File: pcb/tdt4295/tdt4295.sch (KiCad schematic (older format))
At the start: 50 parts

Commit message: minor schematic fixes
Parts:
- gave numbers to parts that had none: 50
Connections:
- net GPIO_LED4 is gone; now on net GPIO_LED3: U101.44 (PE7)
- net GPIO_LED0: now also U101.41 (PE4)
- net GPIO_LED1: now also U101.42 (PE5); no longer U101.41 (PE4)
- net GPIO_LED2: now also U101.43 (PE6); no longer U101.42 (PE5)
- net GPIO_LED3: no longer U101.43 (PE6)
- no-connect marks 16 -> 17

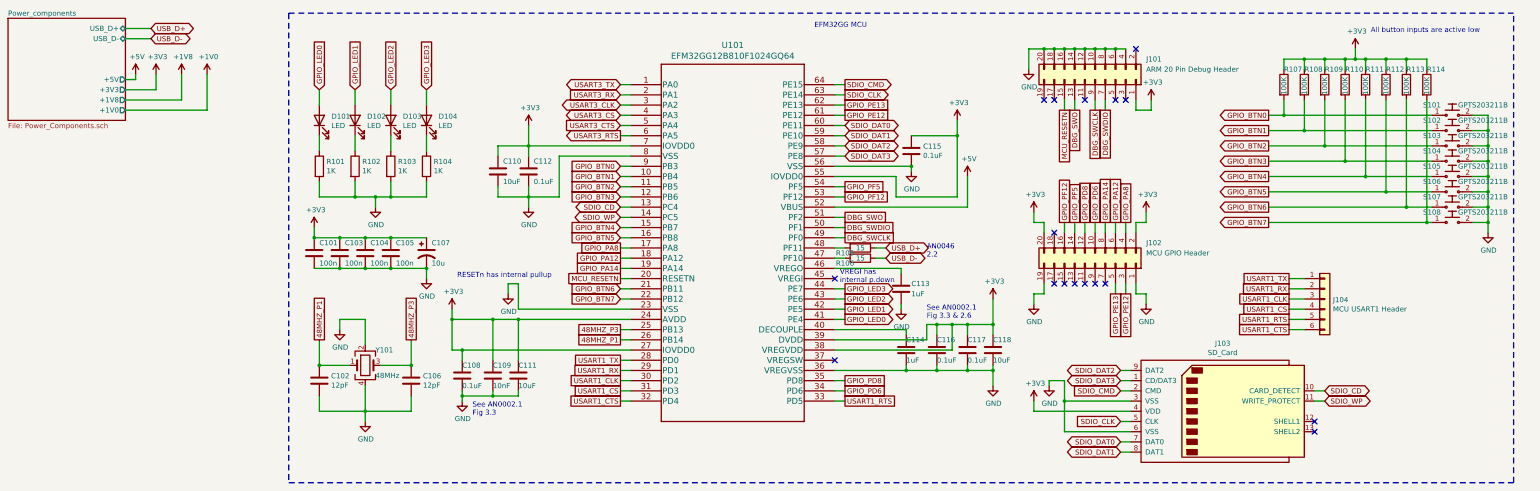
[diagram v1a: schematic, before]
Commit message: Replace PB4-7 with joysticks
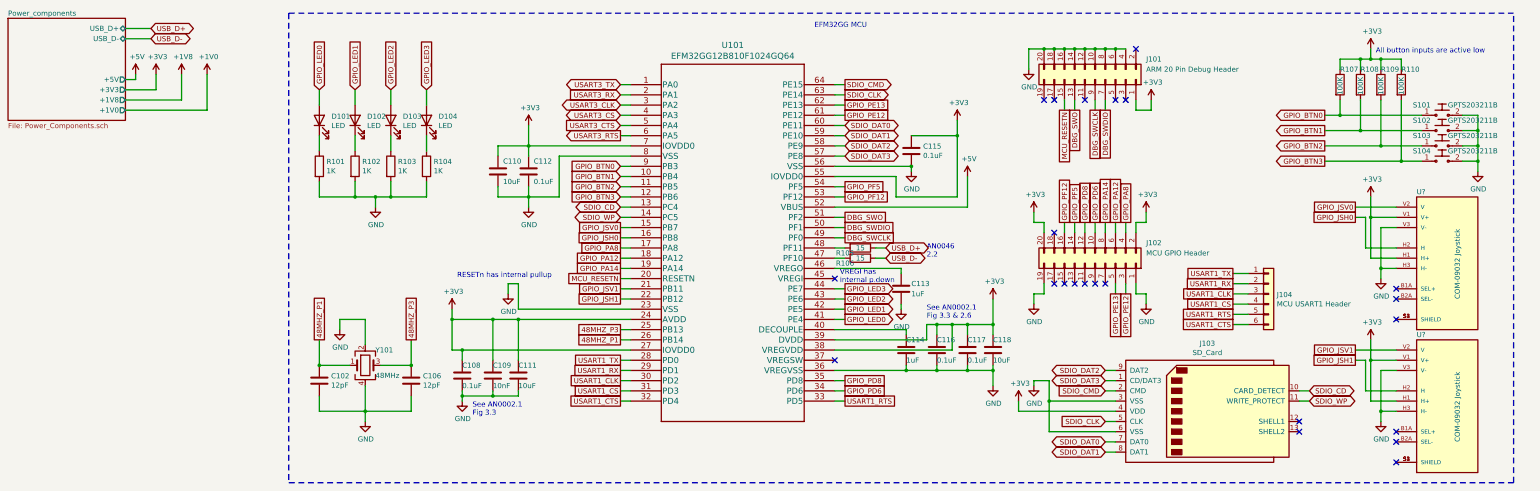
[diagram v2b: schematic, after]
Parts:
- removed C101, C103, C104, C105: 100n, symbol Device:C
- removed C107: 10u, symbol Device:CP1
- removed R111, R112, R113, R114: 100K, symbol Device:R
- removed S105, S106, S107, S108: GPTS203211B, digikey-footprints:PushButton_12x12mm_THT_GPTS203211B, symbol dk_Pushbutton-Switches:GPTS203211B
- added U? (x2): COM-09032 Joystick, XDCR_COM-09032, symbol COM-09032:COM-09032
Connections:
- net +3V3: now also U?.H1 (H+), U?.H1 (H+), U?.V1 (V+), U?.V1 (V+)
- net GND: now also U?.H3 (H-), U?.H3 (H-), U?.V3 (V-), U?.V3 (V-)
- net GPIO_BTN4 renamed GPIO_JSV0
- net GPIO_JSV0: now also U?.V2 (V)
- net GPIO_BTN5 renamed GPIO_JSH0
- net GPIO_JSH0: now also U?.H2 (H)
- net GPIO_BTN6 renamed GPIO_JSV1
- net GPIO_JSV1: now also U?.V2 (V)
- net GPIO_BTN7 renamed GPIO_JSH1
- net GPIO_JSH1: now also U?.H2 (H)
- new net: U?.S1 (SHIELD), U?.S2 (SHIELD), U?.S3 (SHIELD), U?.S4 (SHIELD) (x2)
- no-connect marks 17 -> 23
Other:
- moved on the sheet: J103, J104, R107, R108, R109, R110, S101, S102, S103, S104

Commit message: connect MCU to FPGA
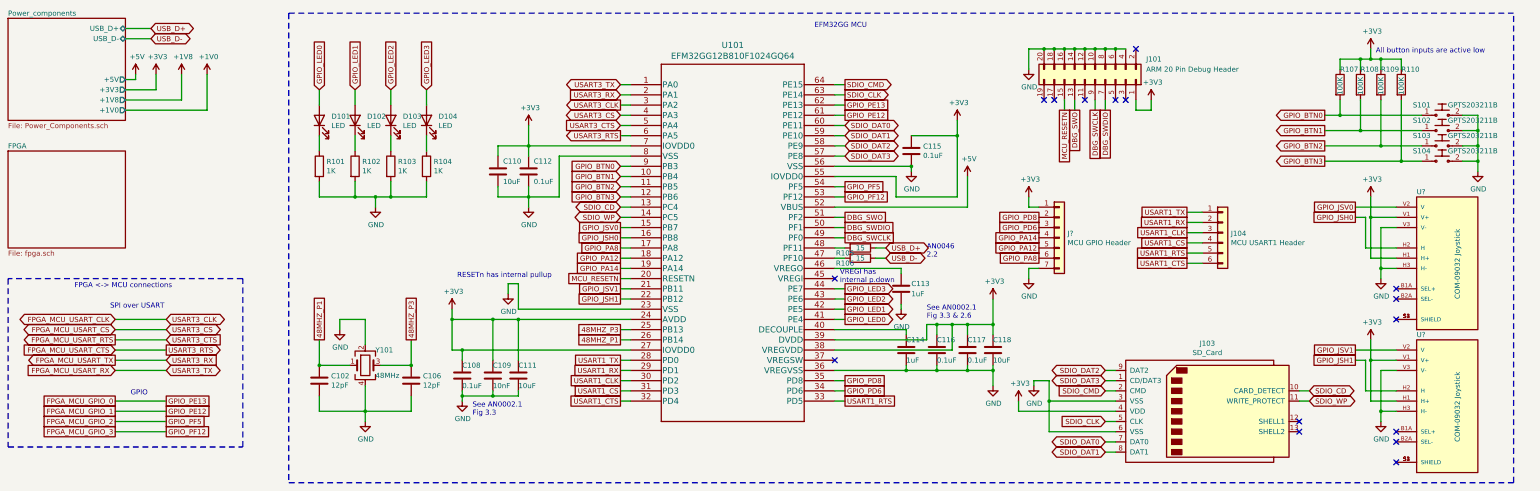
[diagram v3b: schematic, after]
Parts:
- removed J102: MCU GPIO Header, symbol Connector_Generic:Conn_02x10_Odd_Even
- added J?: MCU GPIO Header, symbol Connector_Generic:Conn_01x07
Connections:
- net +3V3: now also J?.1 (Pin_1)
- net GND: now also J?.7 (Pin_7)
- net GPIO_PA12: now also J?.5 (Pin_5)
- net GPIO_PA14: now also J?.4 (Pin_4)
- net GPIO_PA8: now also J?.6 (Pin_6)
- net GPIO_PD6: now also J?.3 (Pin_3)
- net GPIO_PD8: now also J?.2 (Pin_2)
- net GPIO_PE12 renamed FPGA_MCU_GPIO_1
- net GPIO_PE13 renamed FPGA_MCU_GPIO_0
- net GPIO_PF12 renamed FPGA_MCU_GPIO_3
- net GPIO_PF5 renamed FPGA_MCU_GPIO_2
- net USART3_CLK renamed FPGA_MCU_USART_CLK
- net USART3_CS renamed FPGA_MCU_USART_CS
- net USART3_CTS renamed FPGA_MCU_USART_RTS
- net USART3_RTS renamed FPGA_MCU_USART_CTS
- net USART3_RX renamed FPGA_MCU_USART_TX
- net USART3_TX renamed FPGA_MCU_USART_RX
- no-connect marks 23 -> 16
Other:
- note added: "FPGA <-> MCU connections"
- note added: "GPIO"
- note added: "SPI over USART"
- moved on the sheet: J104
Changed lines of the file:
@@
 $Descr A3 16535 11693
 encoding utf-8
-Sheet 1 2
+Sheet 1 7
 Title ""
 Date ""
@@
 Wire Wire Line
 	6150 2300 6850 2300
-$Comp
-L Connector_Generic:Conn_02x10_Odd_Even J102
-U 1 1 6148061B
-P 11400 3350
-F 0 "J102" V 11600 3850 50  0000 L CNN
-F 1 "MCU GPIO Header" V 11500 3850 50  0000 L CNN
-F 2 "" H 11400 3350 50  0001 C CNN
-F 3 "~" H 11400 3350 50  0001 C CNN
-	1    11400 3350
-	0    1    -1   0
-$EndComp
 NoConn ~ 11800 1250
-$Comp
-L power:+3V3 #PWR0116
-U 1 1 6149A7FB
-P 11900 2850
-F 0 "#PWR0116" H 11900 2700 50  0001 C CNN
-F 1 "+3V3" H 11915 3023 50  0000 C CNN
-F 2 "" H 11900 2850 50  0001 C CNN
-F 3 "" H 11900 2850 50  0001 C CNN
-	1    11900 2850
-	1    0    0    -1
-$EndComp
-$Comp
-L power:GND #PWR0117
-U 1 1 6149AFB1
-P 11900 3750
-F 0 "#PWR0117" H 11900 3500 50  0001 C CNN
-F 1 "GND" H 11905 3577 50  0000 C CNN
-F 2 "" H 11900 3750 50  0001 C CNN
-F 3 "" H 11900 3750 50  0001 C CNN
-	1    11900 3750
-	1    0    0    -1
-$EndComp
-Wire Wire Line
-	11800 3650 11800 3550
-Wire Wire Line
-	11800 2950 11800 3050
 Text GLabel 11500 4500 0    50   BiDi ~ 0
 SDIO_DAT3
@@
 	8950 4700 8850 4700
 Wire Wire Line
-	11800 3650 11900 3650
-Wire Wire Line
-	11900 3650 11900 3750
-Wire Wire Line
-	11700 3650 11700 3550
-Wire Wire Line
 	9600 2400 9600 2450
 Wire Wire Line
@@
 Wire Wire Line
 	8950 2700 8850 2700
-Wire Wire Line
-	11800 2950 11900 2950
-Wire Wire Line
-	11900 2950 11900 2850
-Wire Wire Line
-	11700 2950 11700 3050
-Wire Wire Line
-	11600 2950 11600 3050
-Wire Wire Line
-	11500 2950 11500 3050
-Wire Wire Line
-	11400 2950 11400 3050
-Wire Wire Line
-	11300 2950 11300 3050
-Wire Wire Line
-	11200 2950 11200 3050
-Wire Wire Line
-	11100 2950 11100 3050
-$Comp
-L power:+3V3 #PWR0120
-U 1 1 6171BDCE
-P 10800 2850
-F 0 "#PWR0120" H 10800 2700 50  0001 C CNN
-F 1 "+3V3" H 10815 3023 50  0000 C CNN
-F 2 "" H 10800 2850 50  0001 C CNN
-F 3 "" H 10800 2850 50  0001 C CNN
-	1    10800 2850
-	1    0    0    -1
-$EndComp
-Wire Wire Line
-	10900 3050 10900 2950
-Wire Wire Line
-	10900 2950 10800 2950
-Wire Wire Line
-	10800 2950 10800 2850
-$Comp
-L power:GND #PWR0121
-U 1 1 6172366B
-P 10800 3750
-F 0 "#PWR0121" H 10800 3500 50  0001 C CNN
-F 1 "GND" H 10805 3577 50  0000 C CNN
-F 2 "" H 10800 3750 50  0001 C CNN
-F 3 "" H 10800 3750 50  0001 C CNN
-	1    10800 3750
-	1    0    0    -1
-$EndComp
-Wire Wire Line
-	10800 3750 10800 3650
-Wire Wire Line
-	10800 3650 10900 3650
-Wire Wire Line
-	10900 3650 10900 3550
 NoConn ~ 8850 4300
 Wire Notes Line
@@
 Text GLabel 6750 1700 0    50   Input ~ 0
 USART3_RX
-Text GLabel 6750 1800 0    50   BiDi ~ 0
+Text GLabel 6750 1800 0    50   Output ~ 0
 USART3_CLK
 Text GLabel 6750 1900 0    50   BiDi ~ 0
@@
 Text Notes 14150 1300 0    50   ~ 0
 All button inputs are active low
-Wire Wire Line
-	11600 3650 11600 3550
 Text GLabel 8950 1600 2    50   Output ~ 0
 SDIO_CMD
@@
 Wire Wire Line
 	14400 1750 14400 2350
-Text GLabel 11700 2950 1    50   UnSpc ~ 0
-GPIO_PA8
-Text GLabel 11600 2950 1    50   UnSpc ~ 0
-GPIO_PA12
-Text GLabel 11500 2950 1    50   UnSpc ~ 0
+Text GLabel 10850 3100 0    50   UnSpc ~ 0
 GPIO_PA14
-Text GLabel 11400 2950 1    50   UnSpc ~ 0
+Text GLabel 10850 3000 0    50   UnSpc ~ 0
 GPIO_PD6
-Text GLabel 11300 2950 1    50   UnSpc ~ 0
+Text GLabel 10850 2900 0    50   UnSpc ~ 0
 GPIO_PD8
-Text GLabel 11200 2950 1    50   UnSpc ~ 0
-GPIO_PF5
-Text GLabel 11100 2950 1    50   UnSpc ~ 0
-GPIO_PF12
-Text GLabel 11700 3650 3    50   UnSpc ~ 0
-GPIO_PE12
-Text GLabel 11600 3650 3    50   UnSpc ~ 0
-GPIO_PE13
-NoConn ~ 11000 3550
-NoConn ~ 11100 3550
-NoConn ~ 11200 3550
-NoConn ~ 11300 3550
-NoConn ~ 11400 3550
-NoConn ~ 11500 3550
 $Comp
 L Connector_Generic:Conn_01x06 J104
 U 1 1 61BFE8BD
-P 13100 3650
-F 0 "J104" H 13180 3642 50  0000 L CNN
-F 1 "MCU USART1 Header" H 13180 3551 50  0000 L CNN
-F 2 "" H 13100 3650 50  0001 C CNN
-F 3 "~" H 13100 3650 50  0001 C CNN
-	1    13100 3650
-	1    0    0    -1
-$EndComp
-Text GLabel 12750 3450 0    50   UnSpc ~ 0
+P 12650 3050
+F 0 "J104" H 12730 3042 50  0000 L CNN
+F 1 "MCU USART1 Header" H 12730 2951 50  0000 L CNN
+F 2 "" H 12650 3050 50  0001 C CNN
+F 3 "~" H 12650 3050 50  0001 C CNN
+	1    12650 3050
+	1    0    0    -1
+$EndComp
+Text GLabel 12300 2850 0    50   UnSpc ~ 0
 USART1_TX
-Text GLabel 12750 3550 0    50   UnSpc ~ 0
+Text GLabel 12300 2950 0    50   UnSpc ~ 0
 USART1_RX
-Text GLabel 12750 3650 0    50   UnSpc ~ 0
+Text GLabel 12300 3050 0    50   UnSpc ~ 0
 USART1_CLK
-Text GLabel 12750 3750 0    50   UnSpc ~ 0
+Text GLabel 12300 3150 0    50   UnSpc ~ 0
 USART1_CS
-Text GLabel 12750 3850 0    50   UnSpc ~ 0
+Text GLabel 12300 3250 0    50   UnSpc ~ 0
 USART1_RTS
-Text GLabel 12750 3950 0    50   UnSpc ~ 0
+Text GLabel 12300 3350 0    50   UnSpc ~ 0
 USART1_CTS
 Wire Wire Line
-	12750 3450 12900 3450
-Wire Wire Line
-	12900 3550 12750 3550
-Wire Wire Line
-	12750 3650 12900 3650
-Wire Wire Line
-	12900 3750 12750 3750
-Wire Wire Line
-	12750 3850 12900 3850
-Wire Wire Line
-	12900 3950 12750 3950
-NoConn ~ 11000 3050
+	12300 2850 12450 2850
+Wire Wire Line
+	12450 2950 12300 2950
+Wire Wire Line
+	12300 3050 12450 3050
+Wire Wire Line
+	12450 3150 12300 3150
+Wire Wire Line
+	12300 3250 12450 3250
+Wire Wire Line
+	12450 3350 12300 3350
 $Comp
 L power:GND #PWR?
@@
 Wire Wire Line
 	14050 2900 13950 2900
+$Sheet
+S 750  2250 1150 950
+U 617F72AC
+F0 "FPGA" 50
+F1 "fpga.sch" 50
+$EndSheet
+Text GLabel 1800 3900 0    50   BiDi ~ 0
+FPGA_MCU_USART_CLK
+Text GLabel 1800 4000 0    50   BiDi ~ 0
+FPGA_MCU_USART_CS
+Text GLabel 1800 4200 0    50   Input ~ 0
+FPGA_MCU_USART_CTS
+Text GLabel 1800 4100 0    50   Output ~ 0
+FPGA_MCU_USART_RTS
+Text GLabel 1800 4300 0    50   Output ~ 0
+FPGA_MCU_USART_TX
+Text GLabel 1800 4400 0    50   Input ~ 0
+FPGA_MCU_USART_RX
+Text Notes 1750 3800 0    50   ~ 0
+SPI over USART
+Text GLabel 2300 4400 2    50   BiDi ~ 0
+USART3_TX
+Text GLabel 2300 4300 2    50   Input ~ 0
+USART3_RX
+Wire Wire Line
+	2300 4400 1800 4400
+Wire Wire Line
+	1800 4300 2300 4300
+Text GLabel 2300 4200 2    50   Output ~ 0
+USART3_RTS
+Text GLabel 2300 4100 2    50   Input ~ 0
+USART3_CTS
+Text GLabel 2300 4000 2    50   BiDi ~ 0
+USART3_CS
+Text GLabel 2300 3900 2    50   BiDi ~ 0
+USART3_CLK
+Wire Wire Line
+	2300 3900 1800 3900
+Wire Wire Line
+	1800 4000 2300 4000
+Wire Wire Line
+	2300 4100 1800 4100
+Wire Wire Line
+	1800 4200 2300 4200
+Text Notes 1950 4650 0    50   ~ 0
+GPIO
+Wire Notes Line
+	750  3500 750  5150
+Wire Notes Line
+	750  5150 3050 5150
+Wire Notes Line
+	3050 5150 3050 3500
+Wire Notes Line
+	3050 3500 750  3500
+$Comp
+L Connector_Generic:Conn_01x07 J?
+U 1 1 618E52FC
+P 11050 3100
+F 0 "J?" H 11130 3142 50  0000 L CNN
+F 1 "MCU GPIO Header" H 11130 3051 50  0000 L CNN
+F 2 "" H 11050 3100 50  0001 C CNN
+F 3 "~" H 11050 3100 50  0001 C CNN
+	1    11050 3100
+	1    0    0    -1
+$EndComp
+$Comp
+L power:+3V3 #PWR?
+U 1 1 618E6273
+P 10750 2700
+F 0 "#PWR?" H 10750 2550 50  0001 C CNN
+F 1 "+3V3" H 10765 2873 50  0000 C CNN
+F 2 "" H 10750 2700 50  0001 C CNN
+F 3 "" H 10750 2700 50  0001 C CNN
+	1    10750 2700
+	1    0    0    -1
+$EndComp
+Wire Wire Line
+	10750 2700 10750 2800
+Wire Wire Line
+	10750 2800 10850 2800
+$Comp
+L power:GND #PWR?
+U 1 1 618FA27C
+P 10750 3500
+F 0 "#PWR?" H 10750 3250 50  0001 C CNN
+F 1 "GND" H 10755 3327 50  0000 C CNN
+F 2 "" H 10750 3500 50  0001 C CNN
+F 3 "" H 10750 3500 50  0001 C CNN
+	1    10750 3500
+	1    0    0    -1
+$EndComp
+Wire Wire Line
+	10850 3400 10750 3400
+Wire Wire Line
+	10750 3400 10750 3500
+Text GLabel 10850 3200 0    50   UnSpc ~ 0
+GPIO_PA12
+Text GLabel 10850 3300 0    50   UnSpc ~ 0
+GPIO_PA8
+Text GLabel 2300 4700 2    50   UnSpc ~ 0
+GPIO_PE13
+Text GLabel 2300 4800 2    50   UnSpc ~ 0
+GPIO_PE12
+Text GLabel 2300 4900 2    50   UnSpc ~ 0
+GPIO_PF5
+Text GLabel 2300 5000 2    50   UnSpc ~ 0
+GPIO_PF12
+Text GLabel 1800 4700 0    50   UnSpc ~ 0
+FPGA_MCU_GPIO_0
+Text GLabel 1800 4800 0    50   UnSpc ~ 0
+FPGA_MCU_GPIO_1
+Text GLabel 1800 4900 0    50   UnSpc ~ 0
+FPGA_MCU_GPIO_2
+Text GLabel 1800 5000 0    50   UnSpc ~ 0
+FPGA_MCU_GPIO_3
+Wire Wire Line
+	1800 4700 2300 4700
+Wire Wire Line
+	2300 4800 1800 4800
+Wire Wire Line
+	1800 4900 2300 4900
+Wire Wire Line
+	2300 5000 1800 5000
+Text Notes 1400 3600 0    50   ~ 0
+FPGA <-> MCU connections
 $EndSCHEMATC

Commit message: review stuff
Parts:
- added R? (x5): 100, symbol Device:R
- C102, C106: value 12pF -> 14pF
- R101, R102, R103, R104: value 1K -> 330
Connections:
- net GPIO_JSH0: now also U101.19 (PA14); no longer U101.16 (PB8)
- net GPIO_JSH1: now also U101.17 (PA8); no longer U101.22 (PB12)
- net GPIO_JSV0: now also U101.18 (PA12); no longer U101.15 (PB7)
- net GPIO_JSV1: now also U101.34 (PD6); no longer U101.21 (PB11)
- net GPIO_PD8: now also R?.2; no longer J?.2 (Pin_2)
- net GPIO_PA12: no longer names the net of J?.5 (Pin_5)
- net GPIO_PA12: now also R?.1; no longer U101.18 (PA12)
- net GPIO_PA14: no longer names the net of J?.4 (Pin_4)
- net GPIO_PA14: now also R?.1; no longer U101.19 (PA14)
- net GPIO_PA8: no longer names the net of J?.6 (Pin_6)
- net GPIO_PA8: now also R?.1; no longer U101.17 (PA8)
- net GPIO_PD6: no longer names the net of J?.3 (Pin_3)
- net GPIO_PD6: now also R?.1; no longer U101.34 (PD6)
- new net: J?.2 (Pin_2), R?.1
- new net GPIO_PB11: R?.2, U101.21 (PB11)
- new net GPIO_PB12: R?.2, U101.22 (PB12)
- new net GPIO_PB7: R?.2, U101.15 (PB7)
- new net GPIO_PB8: R?.2, U101.16 (PB8)
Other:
- moved on the sheet: J101, J104, J?

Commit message: associate (some) footprints to the symbols
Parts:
- C101: renamed from C102; footprint (none) -> Capacitor_SMD:C_1210_3225Metric_Pad1.33x2.70mm_HandSolder; Category (none) -> C1210C107M9PACTU; DK_Detail_Page (none) -> https://no.farnell.com/kemet/c1210c107m9pactu/cap-100-f-6-3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
- C102: renamed from C106; footprint (none) -> Capacitor_SMD:C_1210_3225Metric_Pad1.33x2.70mm_HandSolder; Category (none) -> C1210C107M9PACTU; DK_Detail_Page (none) -> https://no.farnell.com/kemet/c1210c107m9pactu/cap-100-f-6-3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
- J101: footprint (none) -> Connector_PinHeader_2.54mm:PinHeader_2x10_P2.54mm_Vertical
- J103: renamed from J104; footprint (none) -> Connector_PinSocket_2.54mm:PinSocket_1x06_P2.54mm_Vertical
- J104: renamed from J?; footprint (none) -> Connector_PinSocket_2.54mm:PinSocket_1x07_P2.54mm_Vertical
- R101, R102, R103, R104: footprint (none) -> Resistor_SMD:R_2512_6332Metric_Pad1.40x3.35mm_HandSolder; Component name (none) -> RHC2512FT330R; DK_Detail_Page (none) -> https://www.digikey.no/product-detail/no/stackpole-electron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
- R105, R106: footprint (none) -> Resistor_SMD:R_2512_6332Metric_Pad1.40x3.35mm_HandSolder; Category (none) -> 352215RFT
- R107, R108, R109, R110, R111: renamed from R?; footprint (none) -> Resistor_SMD:R_0805_2012Metric_Pad1.20x1.40mm_HandSolder; Category (none) -> MCU08050C1000FP500; DK_Detail_Page (none) -> https://www.digikey.no/product-detail/no/vishay-beyschlag-d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
- R112: renamed from R107; footprint (none) -> Resistor_SMD:R_0805_2012Metric_Pad1.20x1.40mm_HandSolder; Component name (none) -> RR1220P-104-D; DK_Detail_Page (none) -> https://www.digikey.no/product-detail/no/susumu/RR1220P-104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
- R113: renamed from R108; footprint (none) -> Resistor_SMD:R_0805_2012Metric_Pad1.20x1.40mm_HandSolder; Component name (none) -> RR1220P-104-D; DK_Detail_Page (none) -> https://www.digikey.no/product-detail/no/susumu/RR1220P-104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
- R114: renamed from R109; footprint (none) -> Resistor_SMD:R_0805_2012Metric_Pad1.20x1.40mm_HandSolder; Component name (none) -> RR1220P-104-D; DK_Detail_Page (none) -> https://www.digikey.no/product-detail/no/susumu/RR1220P-104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
- R115: renamed from R110; footprint (none) -> Resistor_SMD:R_0805_2012Metric_Pad1.20x1.40mm_HandSolder; Component name (none) -> RR1220P-104-D; DK_Detail_Page (none) -> https://www.digikey.no/product-detail/no/susumu/RR1220P-104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
- U102, U103: renamed from U?; footprint XDCR_COM-09032 -> com09032-joystick:XDCR_COM-09032
- renumbered C108 to C103, C109 to C104, C110 to C105, C111 to C106, C112 to C107, C113 to C108, C114 to C109, C115 to C110, C116 to C111, C117 to C112, C118 to C113, J103 to J102
